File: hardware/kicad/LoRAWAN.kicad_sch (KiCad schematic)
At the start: 1 part

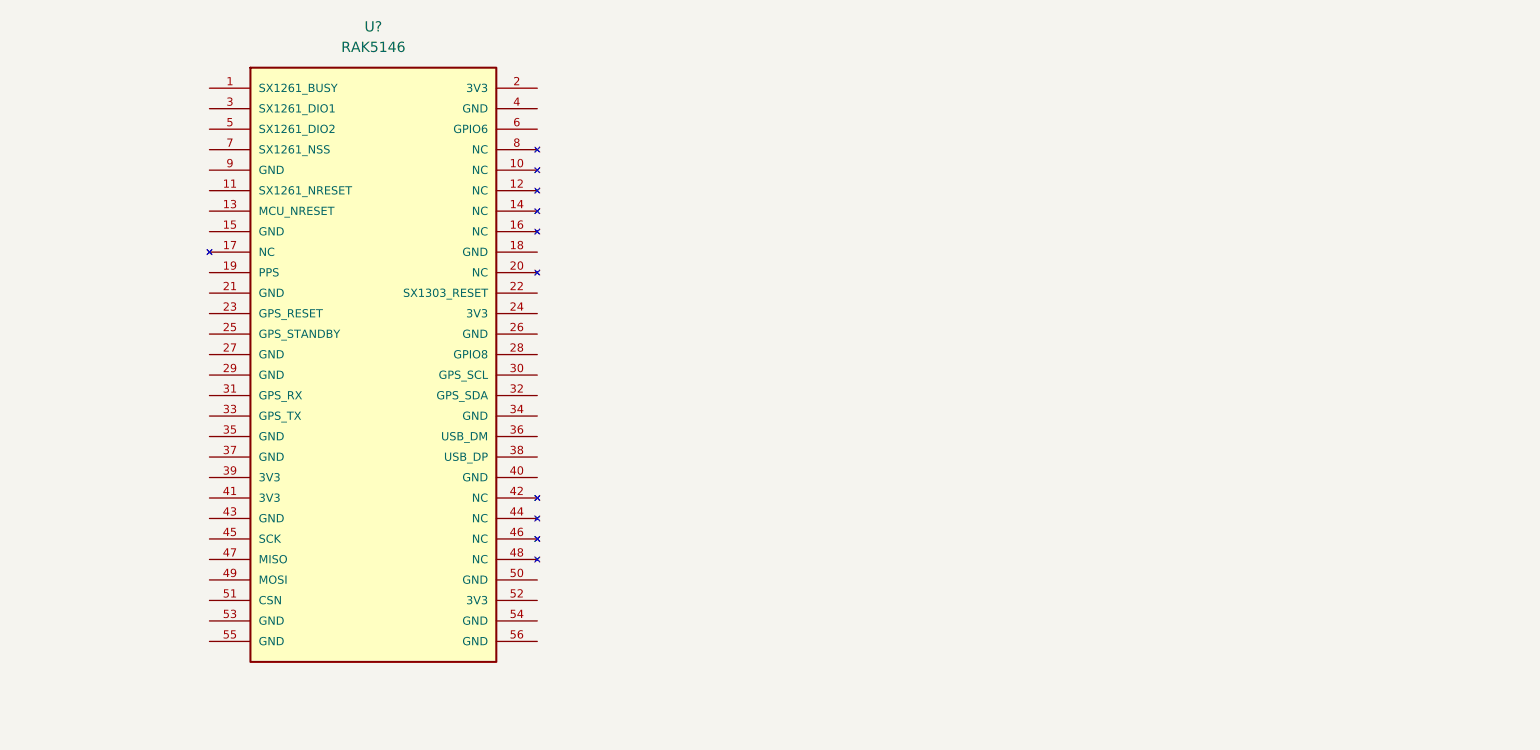
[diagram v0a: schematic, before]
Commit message: update schematic
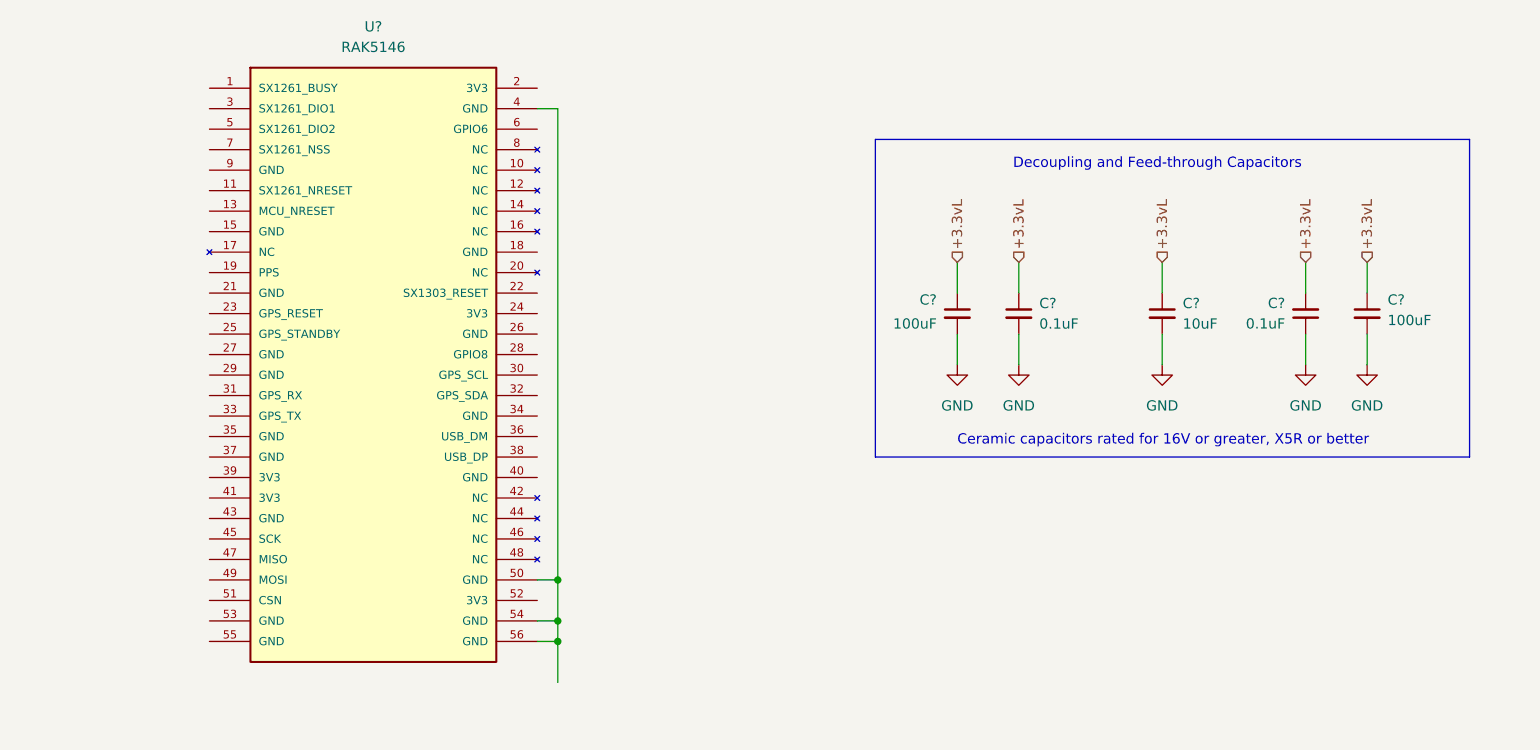
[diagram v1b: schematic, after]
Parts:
- added C? (x2): 0.1uF, symbol Device:C_Small
- added C? (x2): 100uF, symbol Device:C_Small
- added C?: 10uF, symbol Device:C_Small
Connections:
- net at U?.4 (GND): now also U?.50 (GND), U?.54 (GND), U?.56 (GND)
- new net +3.3vL: C?.1, C?.1, C?.1, C?.1, C?.2
- new net GND: C?.1, C?.2, C?.2, C?.2, C?.2
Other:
- note added: "Ceramic capacitors rated for 16V or greater, X5R or better"
- note added: "Decoupling and Feed-through Capacitors"

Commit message: update pcb design
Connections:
- net +3.3vL: now also U?.2 (3V3), U?.24 (3V3), U?.39 (3V3), U?.41 (3V3), U?.52 (3V3)
- net GND: now also U?.15 (GND), U?.18 (GND), U?.21 (GND), U?.26 (GND), U?.27 (GND), U?.29 (GND), U?.34 (GND), U?.35 (GND), U?.37 (GND), U?.4 (GND), U?.40 (GND), U?.43 (GND), U?.50 (GND), U?.53 (GND), U?.54 (GND), U?.55 (GND), U?.56 (GND), U?.9 (GND)
- net LORA_RESET: now reaches U?.22 (SX1303_RESET)
- net GPS_RESET: now reaches U?.23 (GPS_RESET)
- net GPS_STANDBY: now reaches U?.25 (GPS_STANDBY)
- net LORA_GPIO8: now reaches U?.28 (GPIO8)
- net GPS_RXD: now reaches U?.31 (GPS_RX)
- net GPS_TXD: now reaches U?.33 (GPS_TX)
- net LORA_SCK: now reaches U?.45 (SCK)
- net LORA_MISO: now reaches U?.47 (MISO)
- net LORA_MOSI: now reaches U?.49 (MOSI)
- net LORA_CSN: now reaches U?.51 (CSN)
- net LORA_GPIO6: now reaches U?.6 (GPIO6)
- no-connect marks 0 -> 11

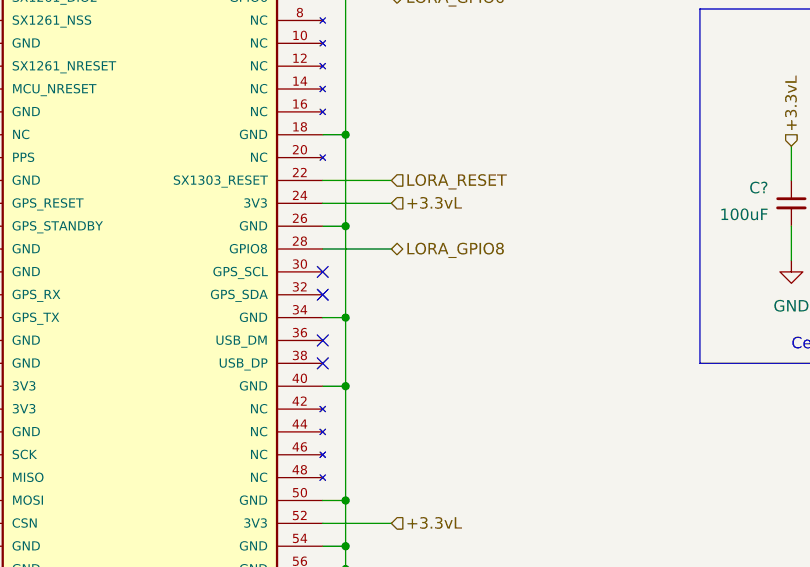
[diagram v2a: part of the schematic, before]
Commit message: breakout GPS I2C
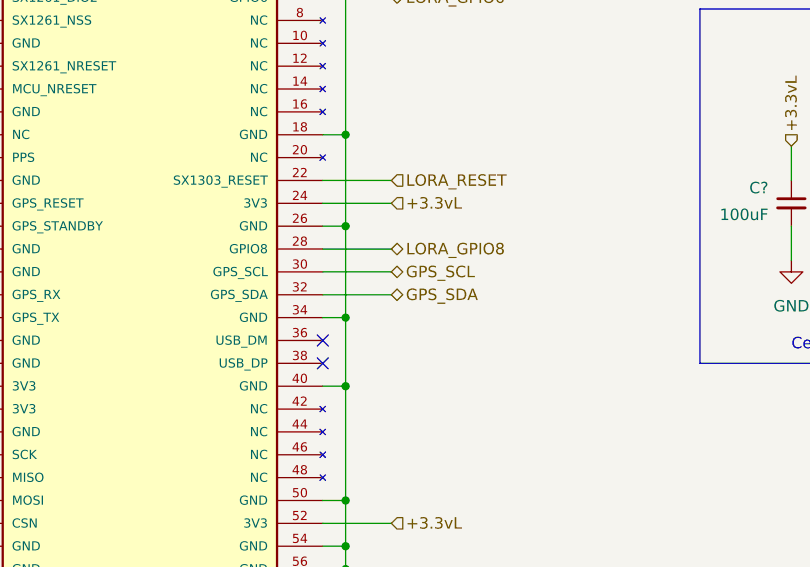
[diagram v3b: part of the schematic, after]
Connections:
- net GPS_SCL: now reaches U?.30 (GPS_SCL)
- net GPS_SDA: now reaches U?.32 (GPS_SDA)
- no-connect marks 11 -> 9
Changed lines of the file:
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@@
   (no_connect (at 92.71 73.66))
   (no_connect (at 92.71 76.2))
-  (no_connect (at 92.71 66.04))
-  (no_connect (at 92.71 68.58))
   (no_connect (at 52.07 43.18))
   (no_connect (at 52.07 45.72))
@@
     (stroke (width 0) (type default) (color 0 0 0 0))
   )
+  (wire (pts (xy 100.33 68.58) (xy 92.71 68.58))
+    (stroke (width 0) (type default) (color 0 0 0 0))
+  )
   (wire (pts (xy 49.53 55.88) (xy 52.07 55.88))
     (stroke (width 0) (type default) (color 0 0 0 0))
@@
   )
   (wire (pts (xy 44.45 60.96) (xy 52.07 60.96))
+    (stroke (width 0) (type default) (color 0 0 0 0))
+  )
+  (wire (pts (xy 100.33 66.04) (xy 92.71 66.04))
     (stroke (width 0) (type default) (color 0 0 0 0))
   )
@@
     (effects (font (size 1.27 1.27)) (justify left))
   )
+  (hierarchical_label "GPS_SCL" (shape bidirectional) (at 100.33 66.04 0)
+    (effects (font (size 1.27 1.27)) (justify left))
+  )
   (hierarchical_label "+3.3vL" (shape input) (at 100.33 58.42 0)
     (effects (font (size 1.27 1.27)) (justify left))
@@
     (effects (font (size 1.27 1.27)) (justify right))
   )
+  (hierarchical_label "GPS_SDA" (shape bidirectional) (at 100.33 68.58 0)
+    (effects (font (size 1.27 1.27)) (justify left))
+  )
   (hierarchical_label "+3.3vL" (shape input) (at 100.33 30.48 0)

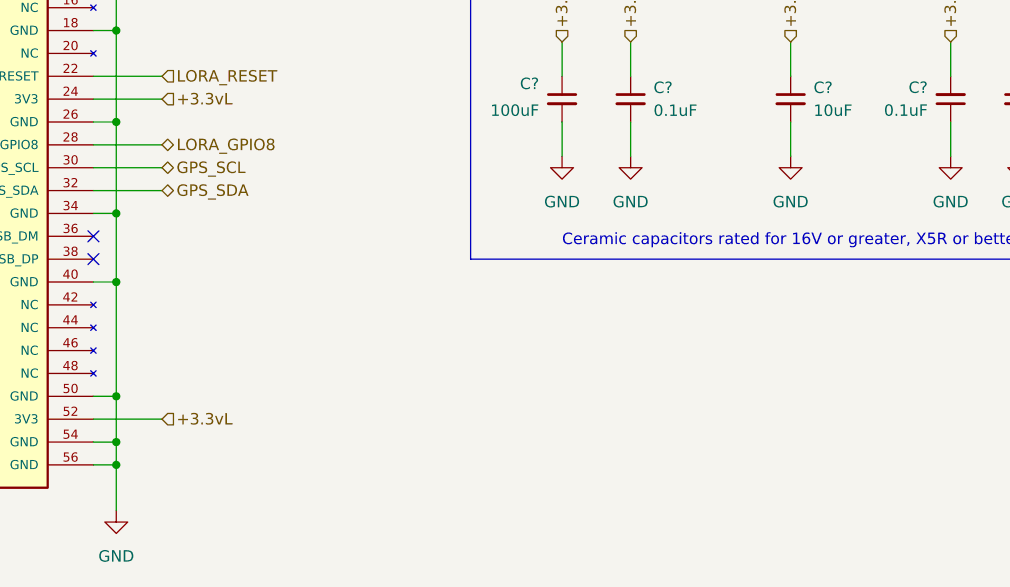
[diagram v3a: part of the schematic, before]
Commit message: wire lorawan and swarm to cm4
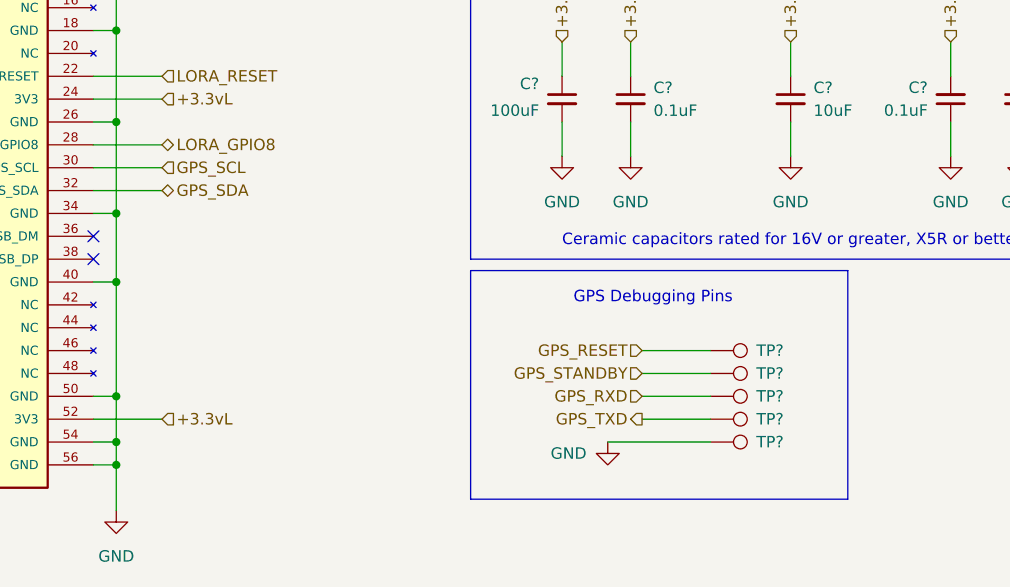
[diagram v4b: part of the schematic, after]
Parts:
- added TP? (x5): ~, symbol Connector:TestPoint
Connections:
- net GND: now also TP?.1
- net GPS_RESET: now also TP?.1
- net GPS_RXD: now also TP?.1
- net GPS_STANDBY: now also TP?.1
- net GPS_TXD: now also TP?.1
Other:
- note added: "GPS Debugging Pins"
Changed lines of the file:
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@@
   (no_connect (at 52.07 35.56))
   (no_connect (at 52.07 38.1))
+  (wire (pts (xy 153.67 91.44) (xy 161.29 91.44))
+    (stroke (width 0) (type default) (color 0 0 0 0))
+  )
   (wire (pts (xy 92.71 78.74) (xy 95.25 78.74))
     (stroke (width 0) (type default) (color 0 0 0 0))
@@
     (stroke (width 0) (type default) (color 0 0 0 0))
   )
+  (polyline (pts (xy 134.62 77.47) (xy 176.53 77.47))
+    (stroke (width 0) (type default) (color 0 0 0 0))
+  )
   (wire (pts (xy 92.71 55.88) (xy 100.33 55.88))
     (stroke (width 0) (type default) (color 0 0 0 0))
@@
     (stroke (width 0) (type default) (color 0 0 0 0))
   )
+  (wire (pts (xy 153.67 86.36) (xy 161.29 86.36))
+    (stroke (width 0) (type default) (color 0 0 0 0))
+  )
   (wire (pts (xy 170.18 52.07) (xy 170.18 55.88))
     (stroke (width 0) (type default) (color 0 0 0 0))
@@
     (stroke (width 0) (type default) (color 0 0 0 0))
   )
+  (wire (pts (xy 153.67 93.98) (xy 161.29 93.98))
+    (stroke (width 0) (type default) (color 0 0 0 0))
+  )
+  (wire (pts (xy 153.67 88.9) (xy 161.29 88.9))
+    (stroke (width 0) (type default) (color 0 0 0 0))
+  )
   (wire (pts (xy 92.71 99.06) (xy 95.25 99.06))
     (stroke (width 0) (type default) (color 0 0 0 0))
@@
     (stroke (width 0) (type default) (color 0 0 0 0))
   )
+  (polyline (pts (xy 176.53 77.47) (xy 176.53 102.87))
+    (stroke (width 0) (type default) (color 0 0 0 0))
+  )
   (wire (pts (xy 44.45 86.36) (xy 52.07 86.36))
     (stroke (width 0) (type default) (color 0 0 0 0))
@@
     (stroke (width 0) (type default) (color 0 0 0 0))
   )
+  (wire (pts (xy 149.86 96.52) (xy 161.29 96.52))
+    (stroke (width 0) (type default) (color 0 0 0 0))
+  )
   (wire (pts (xy 92.71 96.52) (xy 95.25 96.52))
     (stroke (width 0) (type default) (color 0 0 0 0))
@@
     (stroke (width 0) (type default) (color 0 0 0 0))
   )
+  (polyline (pts (xy 134.62 77.47) (xy 134.62 102.87))
+    (stroke (width 0) (type default) (color 0 0 0 0))
+  )
   (wire (pts (xy 95.25 33.02) (xy 95.25 50.8))
     (stroke (width 0) (type default) (color 0 0 0 0))
@@
     (stroke (width 0) (type default) (color 0 0 0 0))
   )
+  (polyline (pts (xy 176.53 102.87) (xy 134.62 102.87))
+    (stroke (width 0) (type default) (color 0 0 0 0))
+  )
   (wire (pts (xy 49.53 83.82) (xy 49.53 96.52))
     (stroke (width 0) (type default) (color 0 0 0 0))
@@
   (polyline (pts (xy 134.62 36.83) (xy 208.28 36.83))
     (stroke (width 0) (type default) (color 0 0 0 0))
+  )
+  (text "GPS Debugging Pins" (at 146.05 81.28 0)
+    (effects (font (size 1.27 1.27)) (justify left bottom))
   )
   (text "Ceramic capacitors rated for 16V or greater, X5R or better"
@@
     (effects (font (size 1.27 1.27)) (justify right))
   )
+  (hierarchical_label "GPS_TXD" (shape output) (at 153.67 93.98 180)
+    (effects (font (size 1.27 1.27)) (justify right))
+  )
   (hierarchical_label "LORA_CSN" (shape input) (at 44.45 93.98 180)
     (effects (font (size 1.27 1.27)) (justify right))
@@
     (effects (font (size 1.27 1.27)) (justify left))
   )
+  (hierarchical_label "GPS_RXD" (shape input) (at 153.67 91.44 180)
+    (effects (font (size 1.27 1.27)) (justify right))
+  )
   (hierarchical_label "LORA_GPIO8" (shape bidirectional) (at 100.33 63.5 0)
     (effects (font (size 1.27 1.27)) (justify left))
   )
-  (hierarchical_label "GPS_SCL" (shape bidirectional) (at 100.33 66.04 0)
+  (hierarchical_label "GPS_RESET" (shape input) (at 153.67 86.36 180)
+    (effects (font (size 1.27 1.27)) (justify right))
+  )
+  (hierarchical_label "GPS_SCL" (shape input) (at 100.33 66.04 0)
     (effects (font (size 1.27 1.27)) (justify left))
   )
@@
   )
   (hierarchical_label "+3.3vL" (shape input) (at 44.45 78.74 180)
+    (effects (font (size 1.27 1.27)) (justify right))
+  )
+  (hierarchical_label "GPS_STANDBY" (shape input) (at 153.67 88.9 180)
     (effects (font (size 1.27 1.27)) (justify right))
   )
@@
     (pin "2")
   )
+  (symbol (lib_id "Connector:TestPoint") (at 161.29 93.98 270) (unit 1)
+    (in_bom yes) (on_board yes)
+    (property "Reference" "TP?" (id 0) (at 166.37 93.98 90)
+      (effects (font (size 1.27 1.27)) (justify left))
+    )
+    (property "Value" "~" (id 1) (at 166.37 95.2499 90)
+      (effects (font (size 1.27 1.27)) (justify left))
+    )
+    (property "Footprint" "" (id 2) (at 161.29 99.06 0)
+      (effects (font (size 1.27 1.27)) hide)
+    )
+    (property "Datasheet" "~" (id 3) (at 161.29 99.06 0)
+      (effects (font (size 1.27 1.27)) hide)
+    )
+    (pin "1")
+  )
   (symbol (lib_id "power:GND") (at 49.53 104.14 0) (unit 1)
     (in_bom yes) (on_board yes) (fields_autoplaced)
@@
     (pin "1")
   )
+  (symbol (lib_id "Connector:TestPoint") (at 161.29 88.9 270) (unit 1)
+    (in_bom yes) (on_board yes)
+    (property "Reference" "TP?" (id 0) (at 166.37 88.9 90)
+      (effects (font (size 1.27 1.27)) (justify left))
+    )
+    (property "Value" "~" (id 1) (at 166.37 90.1699 90)
+      (effects (font (size 1.27 1.27)) (justify left))
+    )
+    (property "Footprint" "" (id 2) (at 161.29 93.98 0)
+      (effects (font (size 1.27 1.27)) hide)
+    )
+    (property "Datasheet" "~" (id 3) (at 161.29 93.98 0)
+      (effects (font (size 1.27 1.27)) hide)
+    )
+    (pin "1")
+  )
+  (symbol (lib_id "Connector:TestPoint") (at 161.29 91.44 270) (unit 1)
+    (in_bom yes) (on_board yes)
+    (property "Reference" "TP?" (id 0) (at 166.37 91.44 90)
+      (effects (font (size 1.27 1.27)) (justify left))
+    )
+    (property "Value" "~" (id 1) (at 166.37 92.7099 90)
+      (effects (font (size 1.27 1.27)) (justify left))
+    )
+    (property "Footprint" "" (id 2) (at 161.29 96.52 0)
+      (effects (font (size 1.27 1.27)) hide)
+    )
+    (property "Datasheet" "~" (id 3) (at 161.29 96.52 0)
+      (effects (font (size 1.27 1.27)) hide)
+    )
+    (pin "1")
+  )
   (symbol (lib_id "power:GND") (at 95.25 104.14 0) (unit 1)
     (in_bom yes) (on_board yes) (fields_autoplaced)
@@
     )
     (property "Datasheet" "" (id 3) (at 95.25 104.14 0)
+      (effects (font (size 1.27 1.27)) hide)
+    )
+    (pin "1")
+  )
+  (symbol (lib_id "Connector:TestPoint") (at 161.29 86.36 270) (unit 1)
+    (in_bom yes) (on_board yes)
+    (property "Reference" "TP?" (id 0) (at 166.37 86.36 90)
+      (effects (font (size 1.27 1.27)) (justify left))
+    )
+    (property "Value" "~" (id 1) (at 173.99 85.09 90)
+      (effects (font (size 1.27 1.27)) (justify left))
+    )
+    (property "Footprint" "" (id 2) (at 161.29 91.44 0)
+      (effects (font (size 1.27 1.27)) hide)
+    )
+    (property "Datasheet" "~" (id 3) (at 161.29 91.44 0)
       (effects (font (size 1.27 1.27)) hide)
     )
@@
     )
     (property "Datasheet" "" (id 3) (at 152.4 64.77 0)
+      (effects (font (size 1.27 1.27)) hide)
+    )
+    (pin "1")
+  )
+  (symbol (lib_id "Connector:TestPoint") (at 161.29 96.52 270) (unit 1)
+    (in_bom yes) (on_board yes)
+    (property "Reference" "TP?" (id 0) (at 166.37 96.52 90)
+      (effects (font (size 1.27 1.27)) (justify left))
+    )
+    (property "Value" "~" (id 1) (at 166.37 97.7899 90)
+      (effects (font (size 1.27 1.27)) (justify left))
+    )
+    (property "Footprint" "" (id 2) (at 161.29 101.6 0)
+      (effects (font (size 1.27 1.27)) hide)
+    )
+    (property "Datasheet" "~" (id 3) (at 161.29 101.6 0)
       (effects (font (size 1.27 1.27)) hide)
     )
@@
       (effects (font (size 1.27 1.27)) hide)
     )
+    (pin "1")
+  )
+  (symbol (lib_id "power:GND") (at 149.86 96.52 0) (unit 1)
+    (in_bom yes) (on_board yes)
+    (property "Reference" "#PWR?" (id 0) (at 149.86 102.87 0)
+      (effects (font (size 1.27 1.27)) hide)
+    )
+    (property "Value" "GND" (id 1) (at 143.51 97.79 0)
+      (effects (font (size 1.27 1.27)) (justify left))
+    )
+    (property "Footprint" "" (id 2) (at 149.86 96.52 0)
+      (effects (font (size 1.27 1.27)) hide)
+    )
+    (property "Datasheet" "" (id 3) (at 149.86 96.52 0)
+      (effects (font (size 1.27 1.27)) hide)
+    )
